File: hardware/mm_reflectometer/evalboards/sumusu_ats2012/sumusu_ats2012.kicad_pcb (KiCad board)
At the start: 4 copper layers, 3 parts, among them J1 Conn_Coaxial, J2 Conn_Coaxial

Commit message: layout of sumusu ats eval board
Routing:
- net Net-(AT1-Pad1): track 0.00 -> 5.97 mm
- net Net-(AT1-Pad2): track 0.00 -> 5.87 mm
- net GND: vias 0 -> 7
- added copper zone on B.Cu, net GND
- added copper zone on F.Cu, net GND
- added copper zone on In1.Cu, net GND
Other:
- board outline added: 19.2 x 13.2 mm
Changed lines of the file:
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@@
 (kicad_pcb (version 20201220) (generator pcbnew)
   (general
-    (thickness 1.6)
+    (thickness 1.7)
   )
   (paper "A4")
@@
       (layer "F.SilkS" (type "Top Silk Screen") (color "White"))
       (layer "F.Paste" (type "Top Solder Paste"))
-      (layer "F.Mask" (type "Top Solder Mask") (color "Green") (thickness 0.01))
-      (layer "F.Cu" (type "copper") (thickness 0.035))
-      (layer "dielectric 1" (type "core") (thickness 0.48) (material "FR4") (epsilon_r 4.5) (loss_tangent 0.02))
-      (layer "In1.Cu" (type "copper") (thickness 0.035))
-      (layer "dielectric 2" (type "prepreg") (thickness 0.48) (material "FR4") (epsilon_r 4.5) (loss_tangent 0.02))
-      (layer "In2.Cu" (type "copper") (thickness 0.035))
-      (layer "dielectric 3" (type "core") (thickness 0.48) (material "FR4") (epsilon_r 4.5) (loss_tangent 0.02))
-      (layer "B.Cu" (type "copper") (thickness 0.035))
-      (layer "B.Mask" (type "Bottom Solder Mask") (color "Green") (thickness 0.01))
+      (layer "F.Mask" (type "Top Solder Mask") (color "Green") (thickness 0.0254))
+      (layer "F.Cu" (type "copper") (thickness 0.03556))
+      (layer "dielectric 1" (type "core") (thickness 0.17018 locked) (material "FR408-HR") (epsilon_r 3.7) (loss_tangent 0.0091))
+      (layer "In1.Cu" (type "copper") (thickness 0.01778))
+      (layer "dielectric 2" (type "prepreg") (thickness 1.1938 locked) (material "FR408-HR") (epsilon_r 3.7) (loss_tangent 0.0091))
+      (layer "In2.Cu" (type "copper") (thickness 0.01778))
+      (layer "dielectric 3" (type "core") (thickness 0.17018 locked) (material "FR408-HR") (epsilon_r 3.7) (loss_tangent 0.0091))
+      (layer "B.Cu" (type "copper") (thickness 0.03556))
+      (layer "B.Mask" (type "Bottom Solder Mask") (color "Green") (thickness 0.0254))
       (layer "B.Paste" (type "Bottom Solder Paste"))
       (layer "B.SilkS" (type "Bottom Silk Screen") (color "White"))
@@
     (property "Sheet name" "")
     (property "mpn" "ATS2012-xxdB-XX")
-    (fp_text reference "AT1" (at -1.27 -5.08 unlocked) (layer "F.SilkS")
+    (fp_text reference "AT1" (at -0.01 -2.1 unlocked) (layer "F.SilkS")
       (effects (font (size 1 1) (thickness 0.15)))
     )
@@
       (net 1 "GND") (pinfunction "Ext"))
   )
+  (gr_rect (start 102.1 107.7) (end 121.25 120.9) (layer "Edge.Cuts") (width 0.05) (fill none))
+  (via (at 111.7 114.3) (size 0.48) (drill 0.254) (layers "F.Cu" "B.Cu") (free) (net 1))
+  (via (at 111.7 114.8) (size 0.48) (drill 0.254) (layers "F.Cu" "B.Cu") (free) (net 1))
+  (via (at 111 114.8) (size 0.48) (drill 0.254) (layers "F.Cu" "B.Cu") (free) (net 1))
+  (via (at 111.7 113.8) (size 0.48) (drill 0.254) (layers "F.Cu" "B.Cu") (free) (net 1))
+  (via (at 112.5 113.8) (size 0.48) (drill 0.254) (layers "F.Cu" "B.Cu") (free) (net 1))
+  (via (at 111 113.8) (size 0.48) (drill 0.254) (layers "F.Cu" "B.Cu") (free) (net 1))
+  (via (at 112.5 114.8) (size 0.48) (drill 0.254) (layers "F.Cu" "B.Cu") (free) (net 1))
+  (segment (start 118.245001 114.3) (end 113.2 114.3) (width 0.39) (layer "F.Cu") (net 2))
+  (segment (start 113.2 114.3) (end 113 114.3) (width 0.39) (layer "F.Cu") (net 2))
+  (segment (start 112.58 114.3) (end 113.2 114.3) (width 0.25) (layer "F.Cu") (net 2))
+  (segment (start 110.94 114.3) (end 110.8 114.3) (width 0.25) (layer "F.Cu") (net 3))
+  (segment (start 109.855 114.3) (end 110.5 114.3) (width 0.39) (layer "F.Cu") (net 3))
+  (segment (start 105.11 114.3) (end 109.855 114.3) (width 0.39) (layer "F.Cu") (net 3))
+  (segment (start 110.5 114.3) (end 110.94 114.3) (width 0.25) (layer "F.Cu") (net 3))
+  (zone (net 1) (net_name "GND") (layer "F.Cu") (hatch edge 0.508)
+    (connect_pads yes (clearance 0.508))
+    (min_thickness 0.254) (filled_areas_thickness no)
+    (fill yes (thermal_gap 0.508) (thermal_bridge_width 0.508))
+    (polygon
+      (pts
+        (xy 112.8 115.1)
+        (xy 110.75 115.1)
+        (xy 110.75 114.6)
+        (xy 112.8 114.6)
+      )
+    )
+  )
+  (zone (net 1) (net_name "GND") (layer "F.Cu") (hatch edge 0.508)
+    (connect_pads yes (clearance 0.508))
+    (min_thickness 0.254) (filled_areas_thickness no)
+    (fill yes (thermal_gap 0.508) (thermal_bridge_width 0.508))
+    (polygon
+      (pts
+        (xy 112.8 114)
+        (xy 110.75 114)
+        (xy 110.75 113.5)
+        (xy 112.8 113.5)
+      )
+    )
+  )
+  (zone (net 1) (net_name "GND") (layers "In1.Cu" "B.Cu") (hatch edge 0.508)
+    (connect_pads yes (clearance 0.508))
+    (min_thickness 0.254) (filled_areas_thickness no)
+    (fill yes (thermal_gap 0.508) (thermal_bridge_width 0.508))
+    (polygon
+      (pts
+        (xy 121.3 120.9)
+        (xy 102 120.9)
+        (xy 102 107.7)
+        (xy 121.3 107.7)
+      )
+    )
+  )
 )

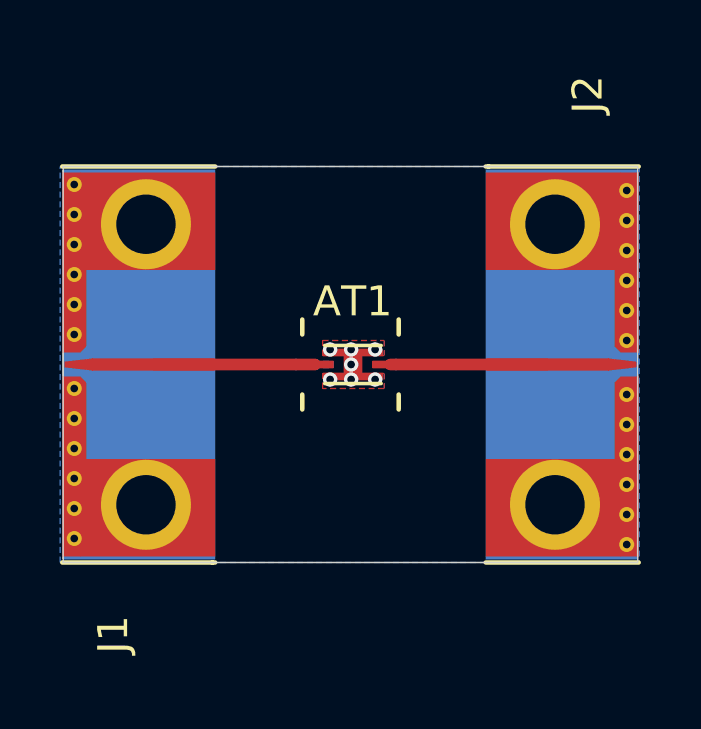
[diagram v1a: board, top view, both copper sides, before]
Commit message: created eval boards for parts on ~8-30 GHz vector reflectometer
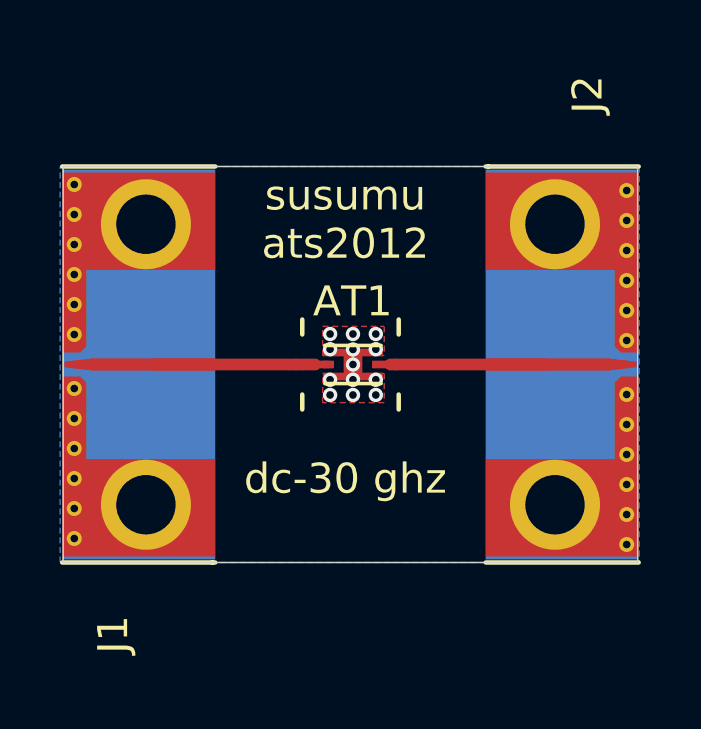
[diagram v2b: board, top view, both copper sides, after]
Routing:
- net GND: vias 7 -> 13
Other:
- board text added: "dc-30 ghz"
- board text added: "susumu ats2012"
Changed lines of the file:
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@@
       (layerselection 0x00010fc_ffffffff)
       (disableapertmacros false)
-      (usegerberextensions false)
+      (usegerberextensions true)
       (usegerberattributes true)
       (usegerberadvancedattributes true)
@@
       (viasonmask false)
       (mode 1)
-      (useauxorigin false)
+      (useauxorigin true)
       (hpglpennumber 1)
       (hpglpenspeed 20)
@@
       (outputformat 1)
       (mirror false)
-      (drillshape 1)
+      (drillshape 0)
       (scaleselection 1)
-      (outputdirectory "")
+      (outputdirectory "plots/")
     )
   )
@@
   )
   (gr_rect (start 102.1 107.7) (end 121.25 120.9) (layer "Edge.Cuts") (width 0.05) (fill none))
-  (via (at 111.7 114.3) (size 0.48) (drill 0.254) (layers "F.Cu" "B.Cu") (free) (net 1))
-  (via (at 111.7 114.8) (size 0.48) (drill 0.254) (layers "F.Cu" "B.Cu") (free) (net 1))
-  (via (at 111 114.8) (size 0.48) (drill 0.254) (layers "F.Cu" "B.Cu") (free) (net 1))
-  (via (at 111.7 113.8) (size 0.48) (drill 0.254) (layers "F.Cu" "B.Cu") (free) (net 1))
-  (via (at 112.5 113.8) (size 0.48) (drill 0.254) (layers "F.Cu" "B.Cu") (free) (net 1))
-  (via (at 111 113.8) (size 0.48) (drill 0.254) (layers "F.Cu" "B.Cu") (free) (net 1))
-  (via (at 112.5 114.8) (size 0.48) (drill 0.254) (layers "F.Cu" "B.Cu") (free) (net 1))
+  (gr_text "dc-30 ghz" (at 111.506 118.11) (layer "F.SilkS")
+    (effects (font (size 1 1) (thickness 0.15)))
+  )
+  (gr_text "susumu\nats2012" (at 111.506 109.474) (layer "F.SilkS")
+    (effects (font (size 1 1) (thickness 0.15)))
+  )
+  (via (at 110.998 113.284) (size 0.48) (drill 0.254) (layers "F.Cu" "B.Cu") (free) (net 1))
+  (via (at 111.76 113.284) (size 0.48) (drill 0.254) (layers "F.Cu" "B.Cu") (free) (net 1))
+  (via (at 111.76 114.3) (size 0.48) (drill 0.254) (layers "F.Cu" "B.Cu") (free) (net 1))
+  (via (at 110.998 115.316) (size 0.48) (drill 0.254) (layers "F.Cu" "B.Cu") (free) (net 1))
+  (via (at 111.76 114.808) (size 0.48) (drill 0.254) (layers "F.Cu" "B.Cu") (free) (net 1))
+  (via (at 111.76 115.316) (size 0.48) (drill 0.254) (layers "F.Cu" "B.Cu") (free) (net 1))
+  (via (at 110.998 114.808) (size 0.48) (drill 0.254) (layers "F.Cu" "B.Cu") (free) (net 1))
+  (via (at 111.76 113.8) (size 0.48) (drill 0.254) (layers "F.Cu" "B.Cu") (free) (net 1))
+  (via (at 112.522 113.284) (size 0.48) (drill 0.254) (layers "F.Cu" "B.Cu") (free) (net 1))
+  (via (at 112.522 113.792) (size 0.48) (drill 0.254) (layers "F.Cu" "B.Cu") (free) (net 1))
+  (via (at 110.998 113.792) (size 0.48) (drill 0.254) (layers "F.Cu" "B.Cu") (free) (net 1))
+  (via (at 112.522 114.808) (size 0.48) (drill 0.254) (layers "F.Cu" "B.Cu") (free) (net 1))
+  (via (at 112.522 115.316) (size 0.48) (drill 0.254) (layers "F.Cu" "B.Cu") (free) (net 1))
   (segment (start 118.245001 114.3) (end 113.2 114.3) (width 0.39) (layer "F.Cu") (net 2))
   (segment (start 113.2 114.3) (end 113 114.3) (width 0.39) (layer "F.Cu") (net 2))
@@
   (segment (start 110.5 114.3) (end 110.94 114.3) (width 0.25) (layer "F.Cu") (net 3))
   (zone (net 1) (net_name "GND") (layer "F.Cu") (hatch edge 0.508)
-    (connect_pads yes (clearance 0.508))
+    (connect_pads yes (clearance 0.1208))
     (min_thickness 0.254) (filled_areas_thickness no)
     (fill yes (thermal_gap 0.508) (thermal_bridge_width 0.508))
     (polygon
       (pts
-        (xy 112.8 115.1)
-        (xy 110.75 115.1)
+        (xy 112.8 115.57)
+        (xy 110.75 115.57)
         (xy 110.75 114.6)
         (xy 112.8 114.6)
@@
   )
   (zone (net 1) (net_name "GND") (layer "F.Cu") (hatch edge 0.508)
-    (connect_pads yes (clearance 0.508))
+    (connect_pads yes (clearance 0.12))
     (min_thickness 0.254) (filled_areas_thickness no)
     (fill yes (thermal_gap 0.508) (thermal_bridge_width 0.508))
@@
         (xy 112.8 114)
         (xy 110.75 114)
-        (xy 110.75 113.5)
-        (xy 112.8 113.5)
+        (xy 110.75 113.03)
+        (xy 112.8 113.03)
       )
     )
   )
   (zone (net 1) (net_name "GND") (layers "In1.Cu" "B.Cu") (hatch edge 0.508)
-    (connect_pads yes (clearance 0.508))
+    (connect_pads yes (clearance 0.1308))
     (min_thickness 0.254) (filled_areas_thickness no)
     (fill yes (thermal_gap 0.508) (thermal_bridge_width 0.508))
